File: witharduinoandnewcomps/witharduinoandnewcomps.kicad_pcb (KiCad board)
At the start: 2 copper layers, 100 x 100 mm, 20 parts, among them J1 FH34SRJ-24S-0.5SH_99_, Q2 ZXM61N03F, Q3 ZXM61N03F, SW1 Button-THT - 2-1825910-7

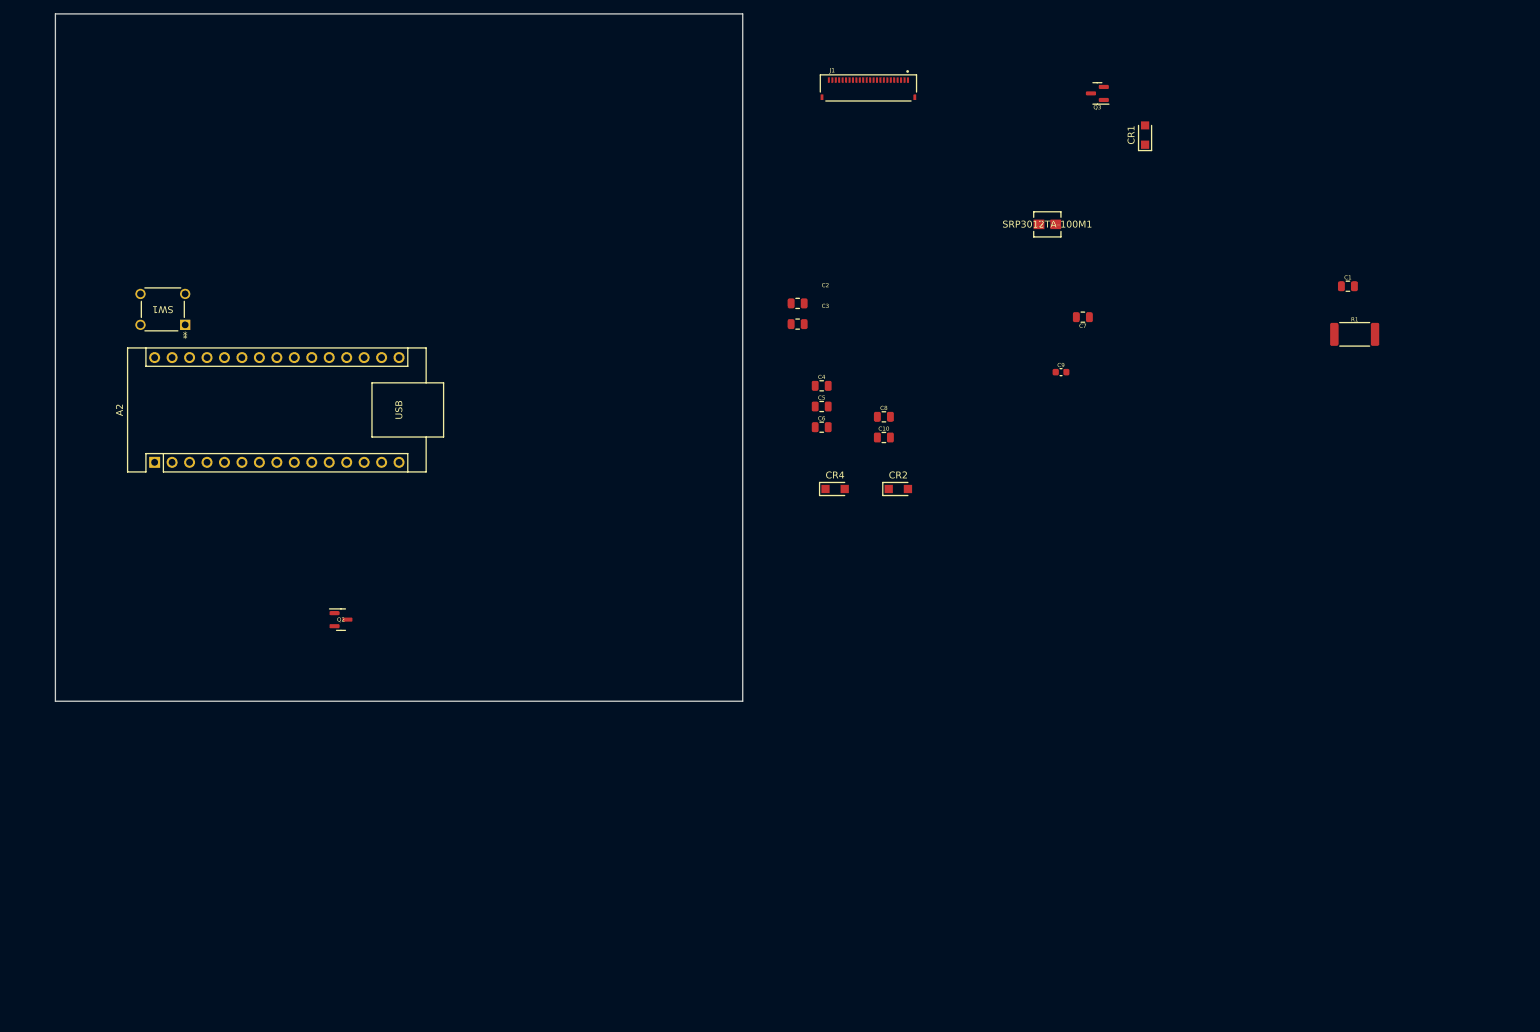
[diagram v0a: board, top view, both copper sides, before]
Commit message: nov 8th changed back to raspberry pico
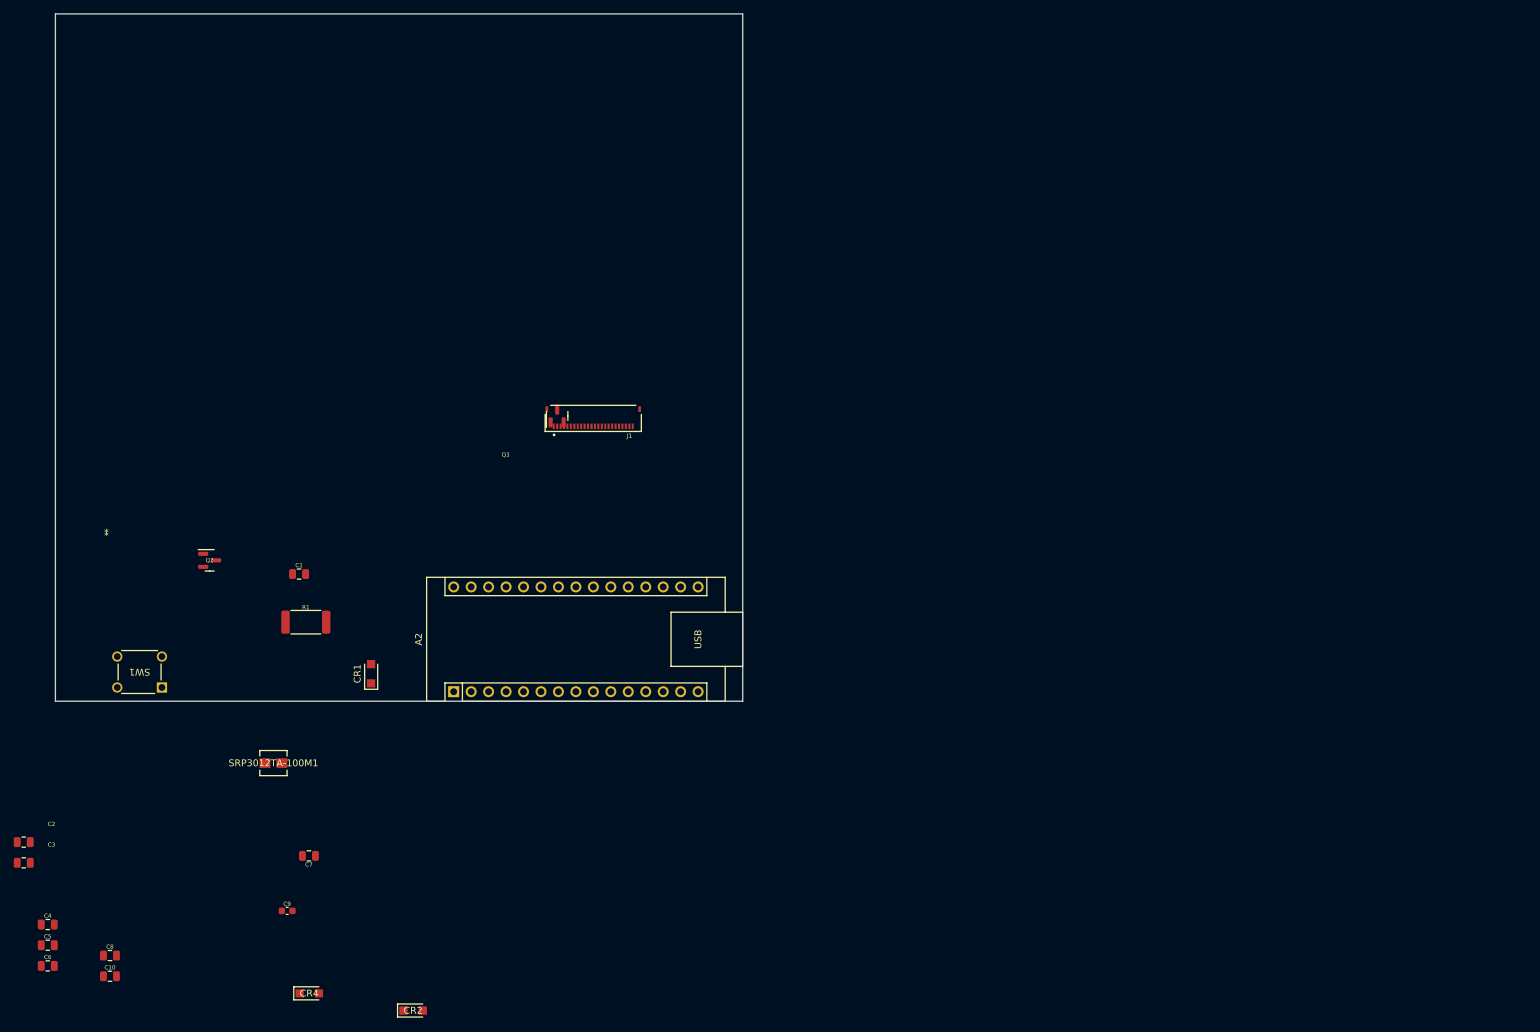
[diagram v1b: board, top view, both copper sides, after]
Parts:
- moved C1 158.2 mm to (61.5, 106.5)
- moved R1 158.2 mm to (62.4, 113.5)
- moved C7 137.2 mm to (62.9, 147.5)
- moved C2 137.2 mm to (21.4, 145.5)
- moved C3 137.2 mm to (21.4, 148.5)
- moved C4 137.2 mm to (24.9, 157.5)
- moved C5 137.2 mm to (24.9, 160.5)
- moved C6 137.2 mm to (24.9, 163.5)
- moved C10 137.2 mm to (33.9, 165.0)
- moved C8 137.2 mm to (33.9, 162.0)
- moved C9 137.2 mm to (59.7, 155.5)
- moved CR1 137.2 mm to (71.9, 121.0)
- moved SRP3012TA-100M1 137.2 mm to (57.7, 134.0)
- moved CR4 106.0 mm to (62.9, 167.5)
- moved CR2 103.6 mm to (78.0, 170.0)
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
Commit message: added new stuff:slow start
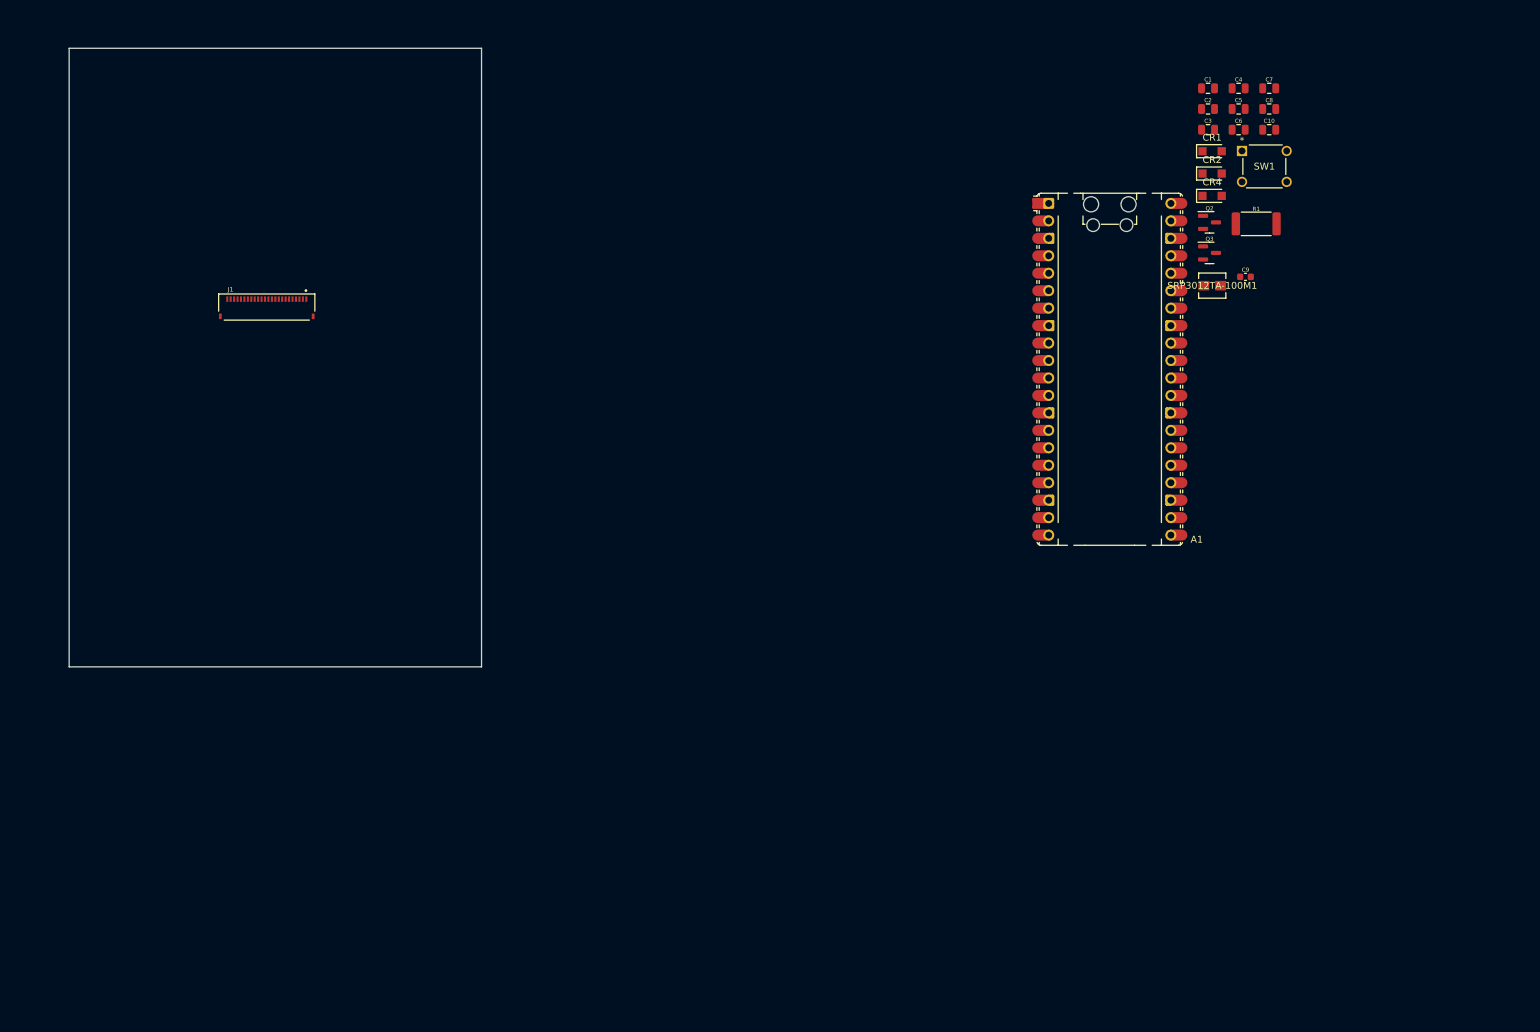
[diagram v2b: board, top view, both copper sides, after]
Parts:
- removed A2: Arduino_Nano_Every, Module:Arduino_Nano
- added A1: RaspberryPi_Pico, Module:RaspberryPi_Pico_Common_Unspecified, F.Cu at (179.4, 76.7)
- moved C4 211.7 mm to (198.2, 35.8)
- moved C5 211.7 mm to (198.2, 38.8)
- moved C6 211.7 mm to (198.2, 41.8)
- moved C10 208.8 mm to (202.6, 41.8)
- moved C8 208.8 mm to (202.6, 38.8)
- moved C2 202.7 mm to (193.7, 38.8)
- moved C3 202.7 mm to (193.7, 41.8)
- moved SW1 183.6 mm to (205.1, 49.4), turned to 0 degrees
- moved C7 178.9 mm to (202.6, 35.8), turned to 0 degrees
- moved CR4 175.3 mm to (194.3, 51.5)
- moved CR2 168.4 mm to (194.3, 48.2)
- moved C9 167.2 mm to (199.2, 63.3)
- moved Q2 153.6 mm to (193.9, 55.3)
- moved SRP3012TA-100M1 153.2 mm to (194.3, 64.5)
- moved C1 149.9 mm to (193.7, 35.8)
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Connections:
- C2 pad 2: Net-(C2-Pad2) -> unconnected-(C2-Pad2)
- C6 pad 2: Net-(C6-Pad2) -> unconnected-(C2-Pad2)
- CR4 pad 2: Net-(C6-Pad2) -> unconnected-(C2-Pad2)
- J1 pad 10: Net-(A2-A2) -> panelReset
- J1 pad 11: Net-(A2-A3) -> panelDC
- J1 pad 12: Net-(A2-MISO) -> unconnected-(J1-Pad12)
- J1 pad 13: Net-(A2-SCL/A5) -> SCL
- J1 pad 14: Net-(A2-SDA/A4) -> SDA
- J1 pad 23: Net-(C6-Pad2) -> unconnected-(C2-Pad2)
- J1 pad 24: Net-(C2-Pad2) -> unconnected-(C2-Pad2)
- J1 pad 8: Net-(A2-A0) -> BS
- J1 pad 9: Net-(A2-A1) -> panelBusy
- J1 pad S1: unconnected-(J1-SHIELD-PadS1) -> unconnected-(C2-Pad2)
- J1 pad S2: unconnected-(J1-SHIELD__1-PadS2) -> unconnected-(C2-Pad2)
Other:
- board size 100 x 100 mm -> 60 x 90 mm

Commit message: Nov22
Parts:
- moved A1 136.8 mm to (44.6, 53.2)
- moved C1 134.4 mm to (68.5, 84.5)
- moved C8 123.1 mm to (107.0, 116.5), turned to -90 degrees
- moved Q3 110.5 mm to (104.5, 124.6), turned to 90 degrees
- moved R1 107.7 mm to (114.0, 119.5), turned to -90 degrees
- moved SRP3012TA-100M1 75.2 mm to (130.3, 104.0)
- moved J1 63.1 mm to (99.8, 113.8), turned to -90 degrees
- moved C6 44.2 mm to (158.8, 62.0)
- moved C9 44.2 mm to (159.8, 83.4)
- moved C10 44.2 mm to (163.2, 62.0)
- moved C2 44.2 mm to (154.3, 59.0)
- moved C3 44.2 mm to (154.3, 62.0)
- moved CR2 42.3 mm to (205.5, 89.0)
- moved C4 38.7 mm to (161.1, 47.0)
- moved C5 38.7 mm to (161.1, 50.0)
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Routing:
- net Net-(Q3-G): track 0.00 -> 7.92 mm
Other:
- board size 60 x 90 mm -> 100 x 100.5 mm

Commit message: laid out pcb
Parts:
- removed C10: 4u7, rsx_capacitors:C_0805_2012Metric
- removed Q2: ZXM61N03F, rsx_packages_TO_SOT:SOT-23
- added C11: 10u, rsx_capacitors:C_0805_2012Metric, F.Cu at (170.6, 96.5)
- added C12: 1u, rsx_capacitors:C_0805_2012Metric, F.Cu at (212.0, 84.5)
- added C13: 1u, rsx_capacitors:C_0805_2012Metric, F.Cu at (218.6, 91.5)
- added C14: 4u7, rsx_capacitors:C_0805_2012Metric, F.Cu at (212.5, 91.5)
- added J3: Screw_Terminal_2x2.54, rsx_headers_screw:Wurth_691210910002, F.Cu at (219.7, 73.0)
- added Q1: ZXM61N03F, rsx_packages_TO_SOT:SOT-23, F.Cu at (167.1, 90.9)
- added R2: 10k, rsx_resistors:R_0603_1608Metric, F.Cu at (166.2, 96.5)
- added R3: 249K_0.1%, rsx_resistors:R_0603_1608Metric, F.Cu at (199.7, 42.5)
- added R4: 1M, rsx_resistors:R_0603_1608Metric, F.Cu at (192.7, 36.5)
- added U1: LDO40LPU33RY, Package_DFN_QFN:DFN-6-1EP_3x3mm_P0.95mm_EP1.7x2.6mm, F.Cu at (213.1, 74.9)
- moved A1 149.8 mm to (194.3, 56.4), turned to 90 degrees
- moved Q3 114.9 mm to (206.1, 71.0), turned to 0 degrees
- moved C1 111.4 mm to (178.9, 70.5)
- moved J1 103.1 mm to (193.8, 71.2), turned to 0 degrees
- moved R1 101.4 mm to (206.0, 77.0), turned to 0 degrees
- moved C8 88.8 mm to (182.9, 70.5), turned to 0 degrees
- moved SRP3012TA-100M1 43.1 mm to (166.8, 81.0), turned to 180 degrees
- moved SW1 41.2 mm to (222.2, 86.3)
- moved CR2 40.3 mm to (167.5, 102.5)
- moved C7 39.6 mm to (168.1, 86.5), turned to 180 degrees
- moved C6 34.1 mm to (175.0, 92.0), turned to -90 degrees
- moved C5 29.7 mm to (177.1, 75.0), turned to 180 degrees
- moved C4 27.3 mm to (174.9, 70.5)
- moved CR1 24.5 mm to (174.6, 81.5), turned to 180 degrees
- moved CR4 22.1 mm to (173.5, 102.5)
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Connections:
- A1 pad 13: GNDPWR -> GND
- A1 pad 18: GNDPWR -> GND
- A1 pad 23: GNDPWR -> GND
- A1 pad 28: GNDPWR -> GND
- A1 pad 3: GNDPWR -> GND
- A1 pad 36: power -> unconnected-(A1-3V3-Pad36)_1
- A1 pad 38: GNDPWR -> GND
- A1 pad 39: Net-(A1-VSYS) -> 3.3v in power
- A1 pad 8: GNDPWR -> GND
- C1 pad 1: GNDPWR -> GND
- C2 pad 1: GNDPWR -> GND
- C2 pad 2: unconnected-(C2-Pad2) -> Net-(C2-Pad2)
- C3 pad 1: GNDPWR -> GND
- C4 pad 1: GNDPWR -> GND
- C5 pad 1: GNDPWR -> GND
- C6 pad 1: GNDPWR -> GND
- C6 pad 2: unconnected-(C2-Pad2) -> Net-(C6-Pad2)
- C7 pad 1: GNDPWR -> GND
- C8 pad 1: GNDPWR -> GND
- C9 pad 2: GNDPWR -> GND
- CR2 pad 1: GNDPWR -> GND
- CR4 pad 2: unconnected-(C2-Pad2) -> Net-(C6-Pad2)
- J1 pad 17: GNDPWR -> GND
- J1 pad 23: unconnected-(C2-Pad2) -> Net-(C6-Pad2)
- J1 pad 24: unconnected-(C2-Pad2) -> Net-(C2-Pad2)
- J1 pad S1: unconnected-(C2-Pad2) -> GND
- J1 pad S2: unconnected-(C2-Pad2) -> GND
- R1 pad 1: GNDPWR -> GND
- SW1 pad 1: power -> +12V
- SW1 pad 2: Net-(A1-VSYS) -> Net-(U1-EN)
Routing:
- net Net-(A1-GPIO26_ADC0): track 0.00 -> 38.3 mm
- net Net-(Q3-G): track 7.92 -> 0.00 mm
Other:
- board size 100 x 100.5 mm -> 60 x 100 mm

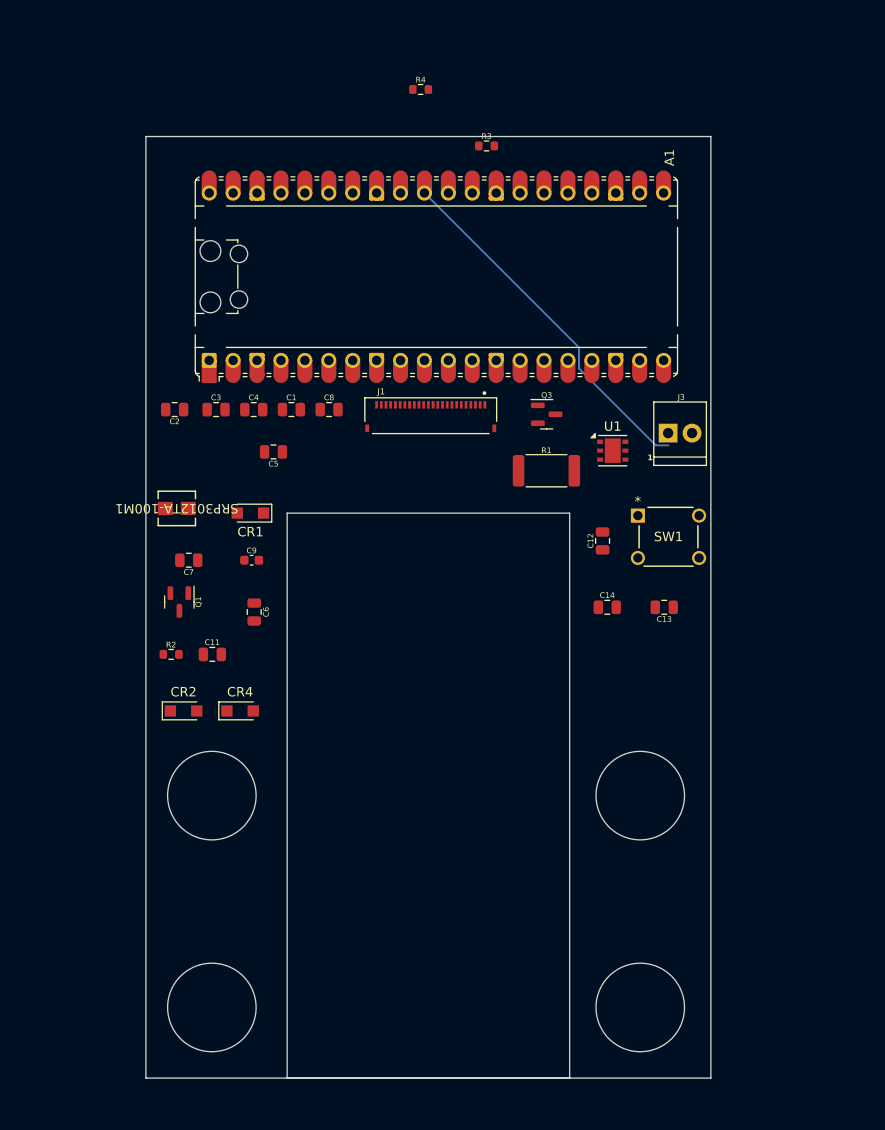
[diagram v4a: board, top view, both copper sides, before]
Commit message: finished routing, ready for submisison (files in folder titled 'submission')
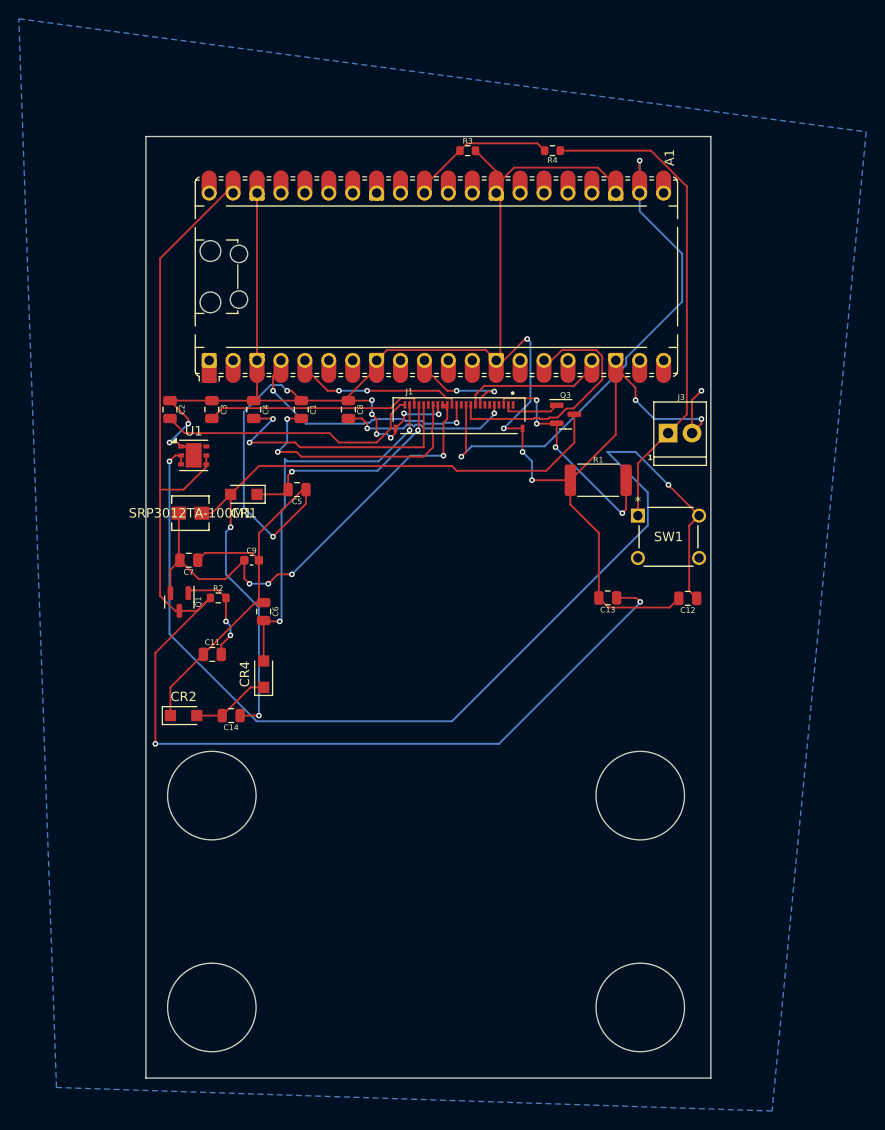
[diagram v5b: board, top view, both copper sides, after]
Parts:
- moved U1 44.5 mm to (168.6, 75.4)
- moved C14 41.6 mm to (172.6, 103.0), turned to 180 degrees
- moved R4 15.4 mm to (206.7, 43.0), turned to 180 degrees
- moved C12 10.9 mm to (221.1, 90.5), turned to 180 degrees
- moved R2 7.81 mm to (171.2, 90.5)
- moved C13 6.08 mm to (212.6, 90.5)
- moved R1 5.59 mm to (211.5, 78.0)
- moved C5 4.72 mm to (179.6, 79.0)
- moved CR4 4.63 mm to (176.0, 98.6), turned to 90 degrees
- moved J1 3.00 mm to (196.8, 71.2)
- moved CR1 2.12 mm to (173.9, 79.5)
- moved R3 2.06 mm to (197.7, 43.0)
- moved C8 2.05 mm to (185.0, 70.5), turned to -90 degrees
- moved Q3 2.00 mm to (208.1, 71.0)
- moved SRP3012TA-100M1 1.52 mm to (168.2, 81.5), turned to 0 degrees
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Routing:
- net GND: track 0.00 -> 273.0 mm, vias 0 -> 17
- net 3.3v in power: track 0.00 -> 138.9 mm, vias 0 -> 2
- net Net-(U1-EN): track 0.00 -> 115.7 mm, vias 0 -> 2
- net Net-(Q3-D): track 0.00 -> 73.2 mm, vias 0 -> 2
- net panelDC: track 0.00 -> 56.8 mm, vias 0 -> 2
- net Net-(Q1-S): track 0.00 -> 53.5 mm, vias 0 -> 4
- net +12V: track 0.00 -> 52.1 mm
- net Net-(C6-Pad2): track 0.00 -> 41.1 mm, vias 0 -> 2
- net Net-(C4-Pad2): track 0.00 -> 28.8 mm, vias 0 -> 2
- net Net-(C2-Pad2): track 0.00 -> 28.5 mm
- net Net-(C1-Pad2): track 0.00 -> 27.1 mm, vias 0 -> 2
- net panelReset: track 0.00 -> 27.0 mm
- net SCL: track 0.00 -> 26.1 mm, vias 0 -> 2
- net Net-(Q3-S): track 0.00 -> 25.2 mm, vias 0 -> 4
- net Net-(C5-Pad2): track 0.00 -> 23.6 mm, vias 0 -> 2
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- added copper zone on B.Cu, net GND
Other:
- outline, holes or cut-outs redrawn
